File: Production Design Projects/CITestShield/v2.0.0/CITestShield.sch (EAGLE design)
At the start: 36 parts, among them CON1 MICRO-SD, IC4 LM75BD, SW1 SPST-4_TP1154_J

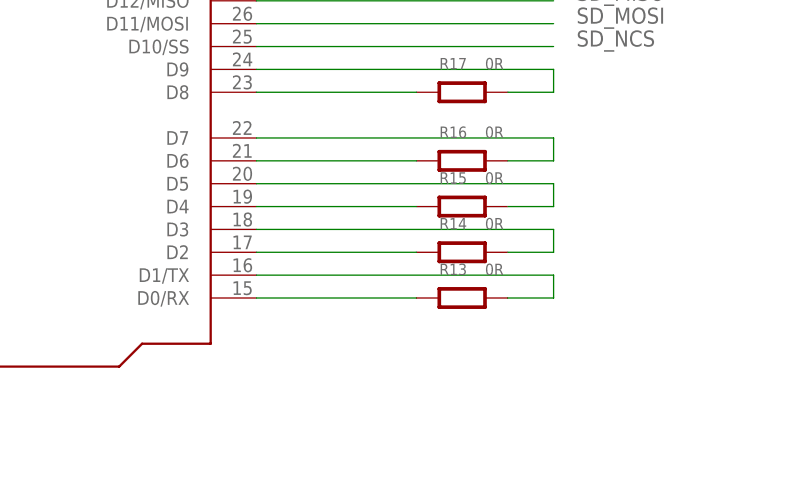
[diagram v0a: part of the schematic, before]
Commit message: Release of v2.0.0 CI test shield, removal of R13(UART Tests Removed)
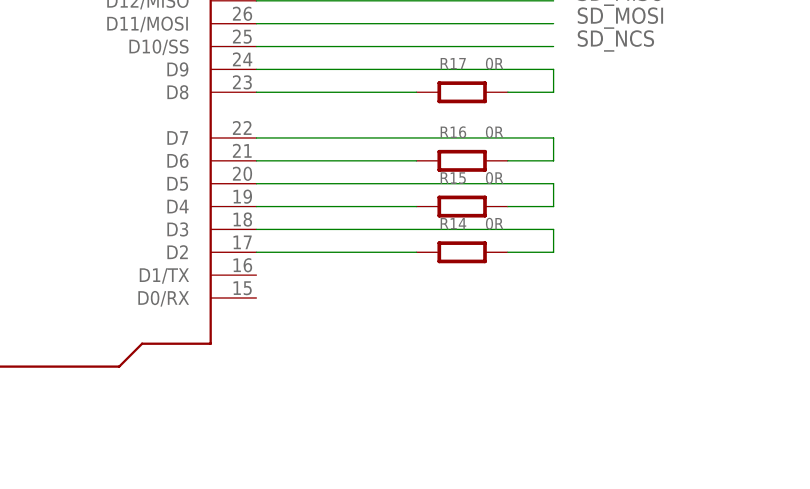
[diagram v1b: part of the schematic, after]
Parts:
- removed R13: 0R, mbed-HDK:R0603
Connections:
- removed net N$12: BRD1.D1/TX, R13.P$2
- removed net N$13: BRD1.D0/RX, R13.P$1
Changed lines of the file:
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@@
 <?xml version="1.0" encoding="utf-8"?>
 <!DOCTYPE eagle SYSTEM "eagle.dtd">
-<eagle version="7.3.0">
+<eagle version="7.6.0">
 <drawing>
 <settings>
@@
 <part name="GND10" library="mbed-HDK" deviceset="GND" device=""/>
 <part name="IC4" library="mbed-HDK" deviceset="LM75BD" device=""/>
-<part name="R13" library="mbed-HDK" deviceset="R" device="0603" value="0R"/>
 <part name="R14" library="mbed-HDK" deviceset="R" device="0603" value="0R"/>
 <part name="R15" library="mbed-HDK" deviceset="R" device="0603" value="0R"/>
@@
 <attribute name="VALUE" x="59.69" y="119.38" size="1.778" layer="96"/>
 </instance>
-<instance part="R13" gate="G$1" x="144.78" y="22.86" smashed="yes">
-<attribute name="NAME" x="142.24" y="25.4" size="1.27" layer="95" font="vector" ratio="12"/>
-<attribute name="VALUE" x="147.32" y="25.4" size="1.27" layer="96" font="vector" ratio="12"/>
-</instance>
 <instance part="R14" gate="G$1" x="144.78" y="27.94" smashed="yes">
 <attribute name="NAME" x="142.24" y="30.48" size="1.27" layer="95" font="vector" ratio="12"/>
@@
 </segment>
 </net>
-<net name="N$12" class="0">
-<segment>
-<pinref part="BRD1" gate="G$1" pin="D1/TX"/>
-<wire x1="121.92" y1="25.4" x2="154.94" y2="25.4" width="0.1524" layer="91"/>
-<wire x1="154.94" y1="25.4" x2="154.94" y2="22.86" width="0.1524" layer="91"/>
-<pinref part="R13" gate="G$1" pin="P$2"/>
-<wire x1="154.94" y1="22.86" x2="149.86" y2="22.86" width="0.1524" layer="91"/>
-</segment>
-</net>
-<net name="N$13" class="0">
-<segment>
-<pinref part="BRD1" gate="G$1" pin="D0/RX"/>
-<pinref part="R13" gate="G$1" pin="P$1"/>
-<wire x1="121.92" y1="22.86" x2="139.7" y2="22.86" width="0.1524" layer="91"/>
-</segment>
-</net>
